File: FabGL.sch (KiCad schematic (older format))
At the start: 30 parts, among them J1 PHX MPT 2.54mm 2pol, J2 Mini-DIN-6, J3 Mini-DIN-6, J4 2.54mm 2x04 straight, J5 IO16/17, J6 DB15_Female_HighDensity, P1 2x40 2.54

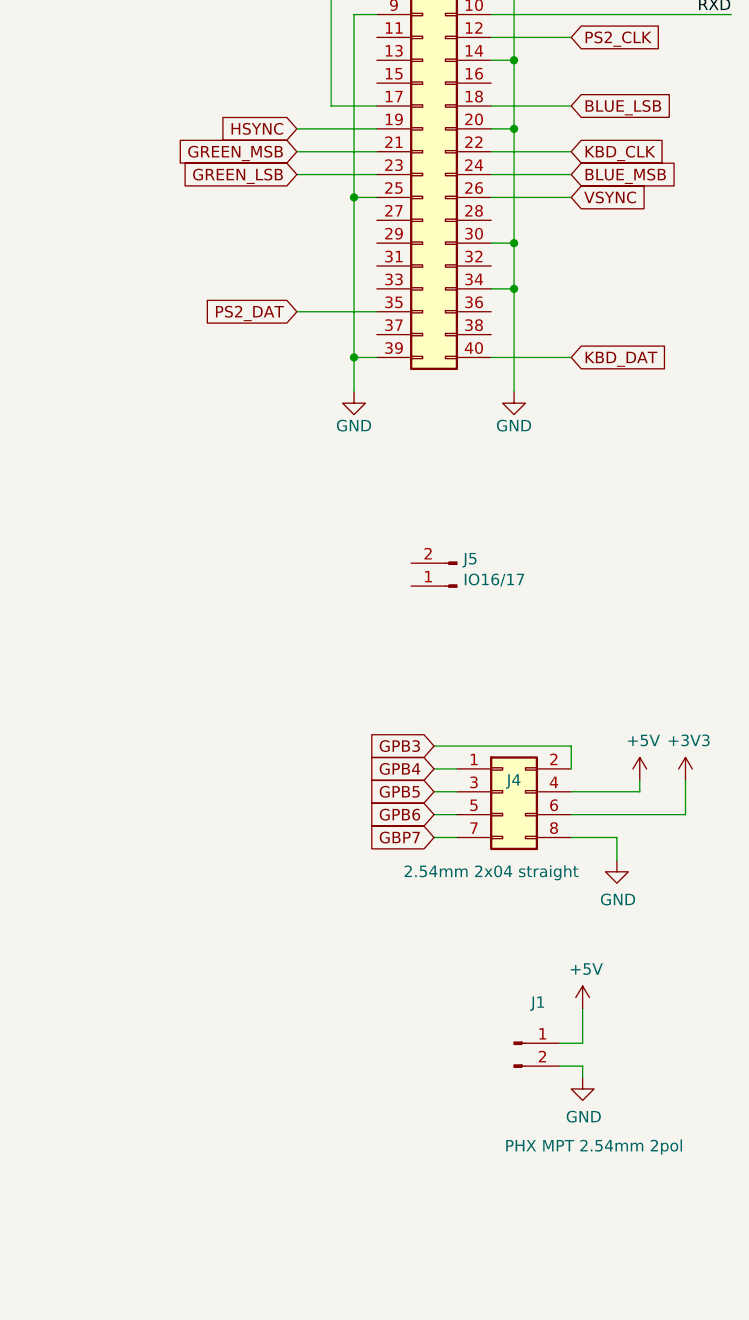
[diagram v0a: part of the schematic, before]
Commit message: Pin swap
Fix pins so the board will boot, correction of error on use of strapping pins
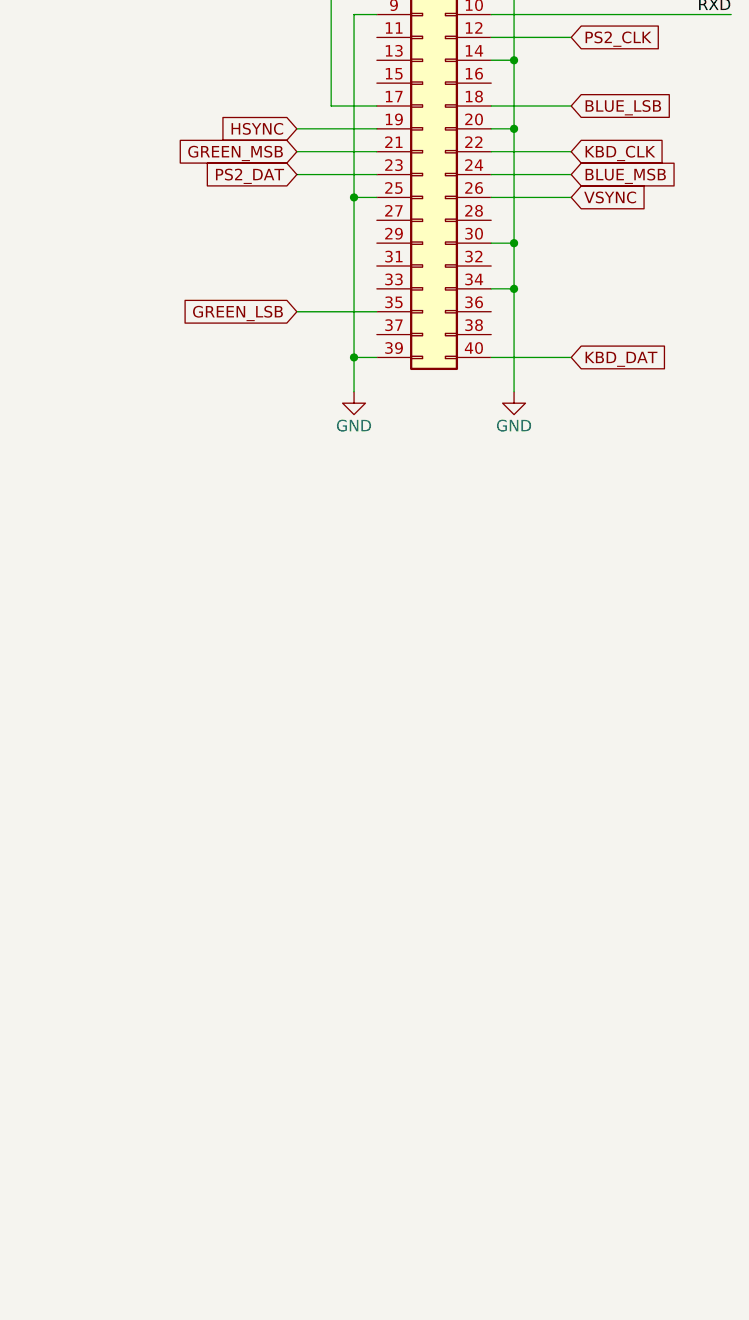
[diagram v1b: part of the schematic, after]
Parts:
- removed J1: PHX MPT 2.54mm 2pol, Socket_Strips:Socket_Strip_Straight_1x02_Pitch2.54mm, symbol Connector:Conn_01x02_Male
- removed J4: 2.54mm 2x04 straight, Socket_Strips:Socket_Strip_Straight_2x04_Pitch2.54mm, symbol Connector_Generic:Conn_02x04_Odd_Even
- removed J5: IO16/17, Socket_Strips:Socket_Strip_Straight_1x02_Pitch2.54mm, symbol Connector:Conn_01x02_Male
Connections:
- net GREEN_LSB: now also P1.35 (Pin_35); no longer P1.23 (Pin_23)
- net PS2_DAT: now also P1.23 (Pin_23); no longer P1.35 (Pin_35)
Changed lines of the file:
@@
 EESchema Schematic File Version 4
+LIBS:FabGL-cache
 EELAYER 29 0
 EELAYER END
@@
 Wire Wire Line
 	10100 1500 10100 1800
-$Comp
-L Connector:Conn_01x02_Male J1
-U 1 1 5C779F05
-P 10100 5800
-F 0 "J1" H 10206 5978 50  0000 C CNN
-F 1 "PHX MPT 2.54mm 2pol" H 10450 5350 50  0000 C CNN
-F 2 "Socket_Strips:Socket_Strip_Straight_1x02_Pitch2.54mm" H 10100 5800 50  0001 C CNN
-F 3 "~" H 10100 5800 50  0001 C CNN
-	1    10100 5800
-	1    0    0    -1
-$EndComp
-$Comp
-L power:GND #PWR07
-U 1 1 5C779F6C
-P 10400 5950
-F 0 "#PWR07" H 10400 5700 50  0001 C CNN
-F 1 "GND" H 10405 5777 50  0000 C CNN
-F 2 "" H 10400 5950 50  0001 C CNN
-F 3 "" H 10400 5950 50  0001 C CNN
-	1    10400 5950
-	1    0    0    -1
-$EndComp
-$Comp
-L power:+5V #PWR06
-U 1 1 5C779FB8
-P 10400 5650
-F 0 "#PWR06" H 10400 5500 50  0001 C CNN
-F 1 "+5V" H 10415 5823 50  0000 C CNN
-F 2 "" H 10400 5650 50  0001 C CNN
-F 3 "" H 10400 5650 50  0001 C CNN
-	1    10400 5650
-	1    0    0    -1
-$EndComp
-Wire Wire Line
-	10300 5800 10400 5800
-Wire Wire Line
-	10400 5800 10400 5650
-Wire Wire Line
-	10300 5900 10400 5900
-Wire Wire Line
-	10400 5900 10400 5950
 Wire Notes Line
 	6950 7150 6950 7750
-$Comp
-L Connector_Generic:Conn_02x04_Odd_Even J4
-U 1 1 5C8F3945
-P 10050 4700
-F 0 "J4" H 10100 4750 50  0000 C CNN
-F 1 "2.54mm 2x04 straight" H 10000 4350 50  0000 C CNN
-F 2 "Socket_Strips:Socket_Strip_Straight_2x04_Pitch2.54mm" H 10050 4700 50  0001 C CNN
-F 3 "~" H 10050 4700 50  0001 C CNN
-	1    10050 4700
-	1    0    0    -1
-$EndComp
-Wire Wire Line
-	10350 4600 10350 4500
-Wire Wire Line
-	10350 4700 10650 4700
-Wire Wire Line
-	10350 4800 10850 4800
-$Comp
-L power:GND #PWR047
-U 1 1 5C98B933
-P 10550 5000
-F 0 "#PWR047" H 10550 4750 50  0001 C CNN
-F 1 "GND" H 10555 4827 50  0000 C CNN
-F 2 "" H 10550 5000 50  0001 C CNN
-F 3 "" H 10550 5000 50  0001 C CNN
-	1    10550 5000
-	1    0    0    -1
-$EndComp
-Wire Wire Line
-	10550 5000 10550 4900
-Wire Wire Line
-	10550 4900 10350 4900
-$Comp
-L Connector:Conn_01x02_Male J5
-U 1 1 5CD4C13F
-P 9850 3800
-F 0 "J5" H 9822 3682 50  0000 R CNN
-F 1 "IO16/17" H 9822 3773 50  0000 R CNN
-F 2 "Socket_Strips:Socket_Strip_Straight_1x02_Pitch2.54mm" H 9850 3800 50  0001 C CNN
-F 3 "~" H 9850 3800 50  0001 C CNN
-	1    9850 3800
-	-1   0    0    1
-$EndComp
-$Comp
-L power:+3V3 #PWR0102
-U 1 1 5CE6F109
-P 10850 4650
-F 0 "#PWR0102" H 10850 4500 50  0001 C CNN
-F 1 "+3V3" H 10865 4823 50  0000 C CNN
-F 2 "" H 10850 4650 50  0001 C CNN
-F 3 "" H 10850 4650 50  0001 C CNN
-	1    10850 4650
-	1    0    0    -1
-$EndComp
-$Comp
-L power:+5V #PWR0103
-U 1 1 5CE6F113
-P 10650 4650
-F 0 "#PWR0103" H 10650 4500 50  0001 C CNN
-F 1 "+5V" H 10665 4823 50  0000 C CNN
-F 2 "" H 10650 4650 50  0001 C CNN
-F 3 "" H 10650 4650 50  0001 C CNN
-	1    10650 4650
-	1    0    0    -1
-$EndComp
-Wire Wire Line
-	10650 4700 10650 4650
-Wire Wire Line
-	10850 4800 10850 4650
-Text GLabel 9750 4500 0    50   Input ~ 0
-GPB3
-Wire Wire Line
-	10350 4500 9750 4500
-Text GLabel 9750 4600 0    50   Input ~ 0
-GPB4
-Text GLabel 9750 4700 0    50   Input ~ 0
-GPB5
-Text GLabel 9750 4800 0    50   Input ~ 0
-GPB6
-Text GLabel 9750 4900 0    50   Input ~ 0
-GBP7
-Wire Wire Line
-	9750 4600 9850 4600
-Wire Wire Line
-	9750 4700 9850 4700
-Wire Wire Line
-	9750 4800 9850 4800
-Wire Wire Line
-	9750 4900 9850 4900
 $Comp
 L Connector:DB15_Female_HighDensity J6
@@
 Text GLabel 9150 1900 0    50   Input ~ 0
 GREEN_MSB
-Text GLabel 9150 2000 0    50   Input ~ 0
+Text GLabel 9150 2600 0    50   Input ~ 0
 GREEN_LSB
 Text GLabel 10350 2000 2    50   Input ~ 0
@@
 Text GLabel 10350 1400 2    50   Input ~ 0
 PS2_CLK
-Text GLabel 9150 2600 0    50   Input ~ 0
+Text GLabel 9150 2000 0    50   Input ~ 0
 PS2_DAT
 Wire Wire Line
